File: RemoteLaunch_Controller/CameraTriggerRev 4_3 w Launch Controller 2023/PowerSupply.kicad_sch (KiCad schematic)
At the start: 20 parts, among them J1 Pwr switch, J10 SW, J11 pwr, U1 AMS1117CD-5.0

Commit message: Adding Rev4_3 rev
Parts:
- added H5: (no value), MountingHole:MountingHole_3.7mm_Pad, symbol Mechanical:MountingHole_Pad
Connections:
- net GND: now also H5.1
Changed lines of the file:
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@@
+    )
+  )
+  (symbol (lib_id "power:GND") (at 85.09 129.54 0) (unit 1)
+    (in_bom yes) (on_board yes) (dnp no)
+    (property "Reference" "#PWR049" (at 85.09 135.89 0)
+      (effects (font (size 1.27 1.27)) hide)
+    )
+    (property "Value" "GND" (at 85.217 133.9342 0)
+      (effects (font (size 1.27 1.27)))
+    )
+    (property "Footprint" "" (at 85.09 129.54 0)
+      (effects (font (size 1.27 1.27)) hide)
+    )
+    (property "Datasheet" "" (at 85.09 129.54 0)
+      (effects (font (size 1.27 1.27)) hide)
+    )
+    (pin "1")
+    (instances
+      (project "CameraTriggerSensorNodeOnly"
+        (path "/be0400c2-1232-4f08-847a-2fb9cb6273cc/00000000-0000-0000-0000-00006220007f"
+          (reference "#PWR049") (unit 1)
+        )
+      )
+    )
+  )
+  (symbol (lib_id "Mechanical:MountingHole_Pad") (at 85.09 127 0) (unit 1)
+    (in_bom yes) (on_board yes) (dnp no)
+    (property "Reference" "H5" (at 87.63 125.7554 0)
+      (effects (font (size 1.27 1.27)) (justify left))
+    )
+    (property "Value" " " (at 87.63 128.0668 0)
+      (effects (font (size 1.27 1.27)) (justify left))
+    )
+    (property "Footprint" "MountingHole:MountingHole_3.7mm_Pad" (at 85.09 127 0)
+      (effects (font (size 1.27 1.27)) hide)
+    )
+    (property "Datasheet" "~" (at 85.09 127 0)
+      (effects (font (size 1.27 1.27)) hide)
+    )
+    (pin "1")
+    (instances
+      (project "CameraTriggerSensorNodeOnly"
+        (path "/be0400c2-1232-4f08-847a-2fb9cb6273cc/00000000-0000-0000-0000-00006220007f"
+          (reference "H5") (unit 1)
+        )
+      )
     )
   )

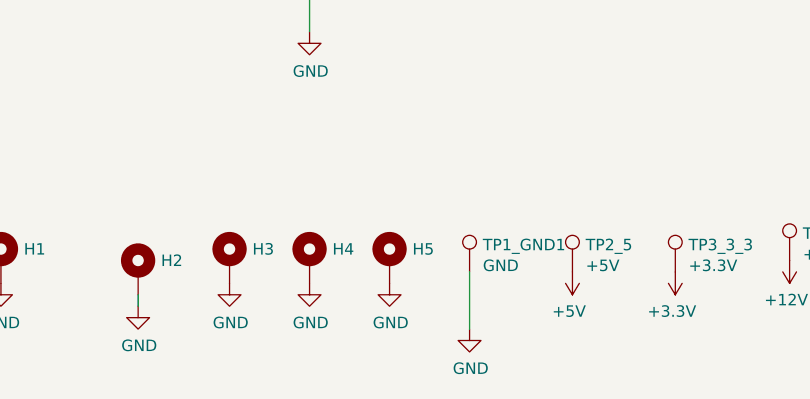
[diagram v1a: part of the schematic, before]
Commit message: Working on adding polling / heartbeat;  Seem to have broken launch
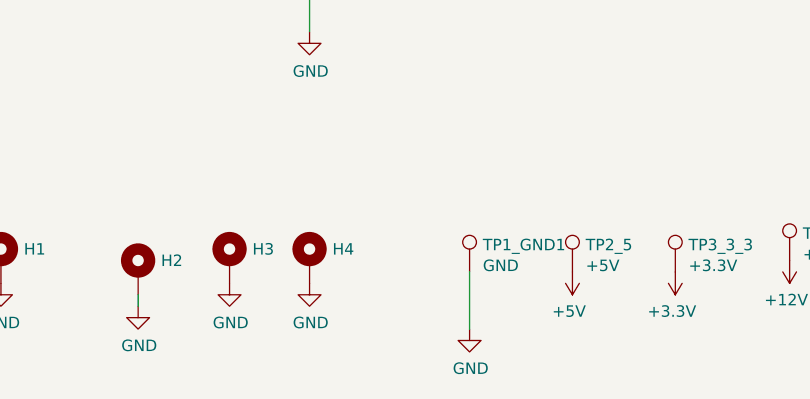
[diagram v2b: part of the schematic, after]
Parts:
- removed H5: (no value), MountingHole:MountingHole_3.7mm_Pad, symbol Mechanical:MountingHole_Pad
